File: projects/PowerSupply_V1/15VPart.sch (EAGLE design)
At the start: 24 parts, among them IC1 LM2596T, IC2 LM2596T, X1 IN, X2 OUT

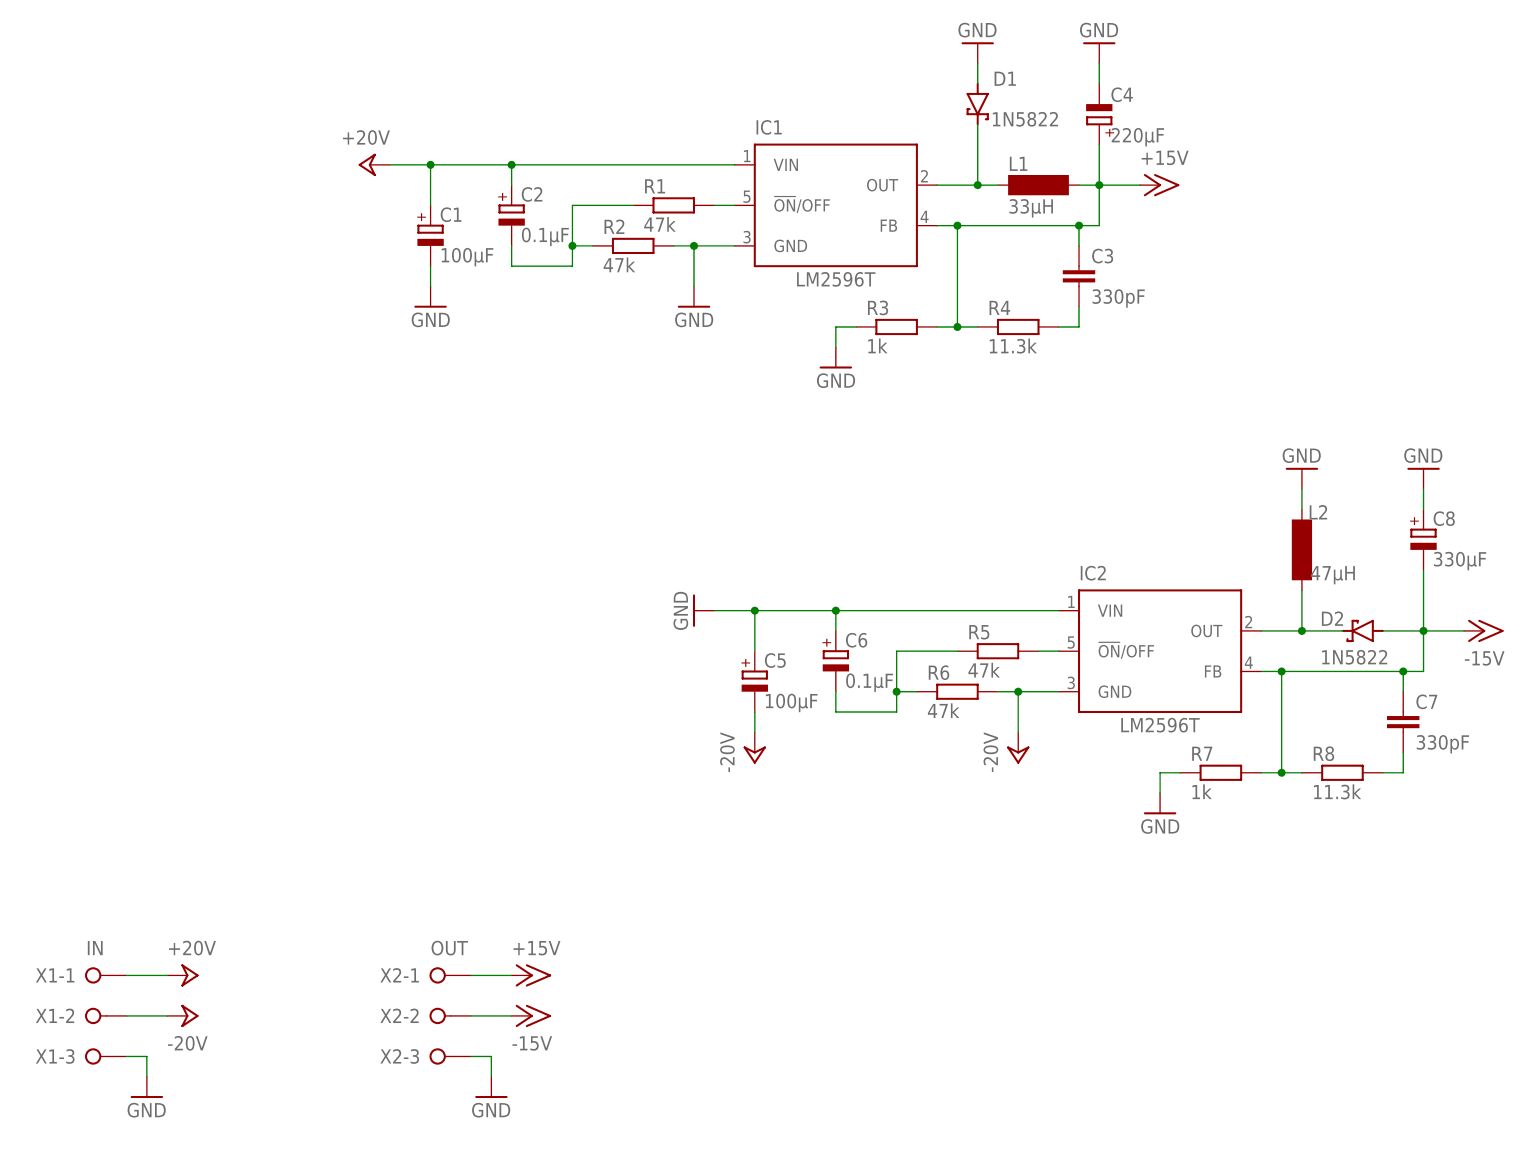
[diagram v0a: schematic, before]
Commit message: refactor(15v): schematics and routing changed
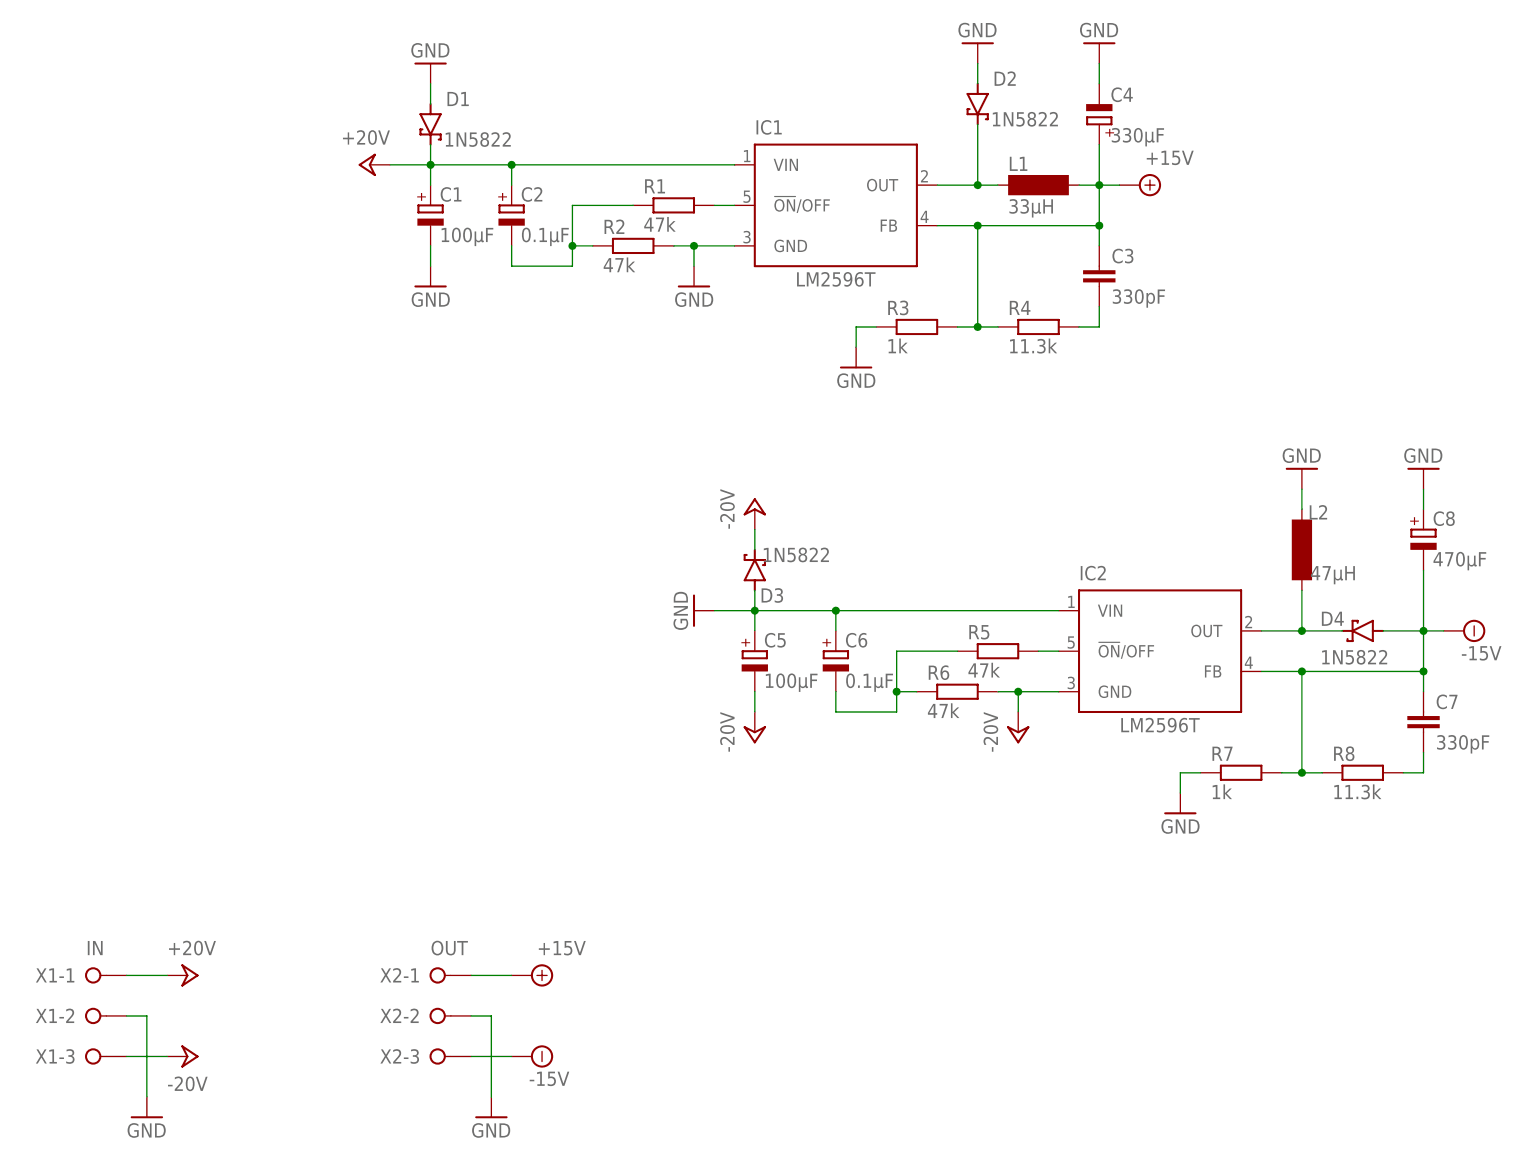
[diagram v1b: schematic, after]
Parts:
- added D3, D4: 1N5822, diode:SCHOTTKY-DIODEC4111-15
- C4: value 220µF -> 330µF
- C8: value 330µF -> 470µF
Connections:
- net +24V: now also D1.C
- net -15V: now also D4.A, X2-3.KL; no longer D2.A, X2-2.KL
- net -24V: now also D3.C, X1-3.KL; no longer X1-2.KL
- net GND: now also D2.A, D3.A, X1-2.KL, X2-2.KL; no longer X1-3.KL, X2-3.KL
- net N$2: now also D4.C; no longer D2.C
- net N$3: now also D2.C; no longer D1.C
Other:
- moved on the sheet: C1, C3, C5, C7, D1, D2, R3, R4, R7, R8

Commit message: feat: 15VPart refactored
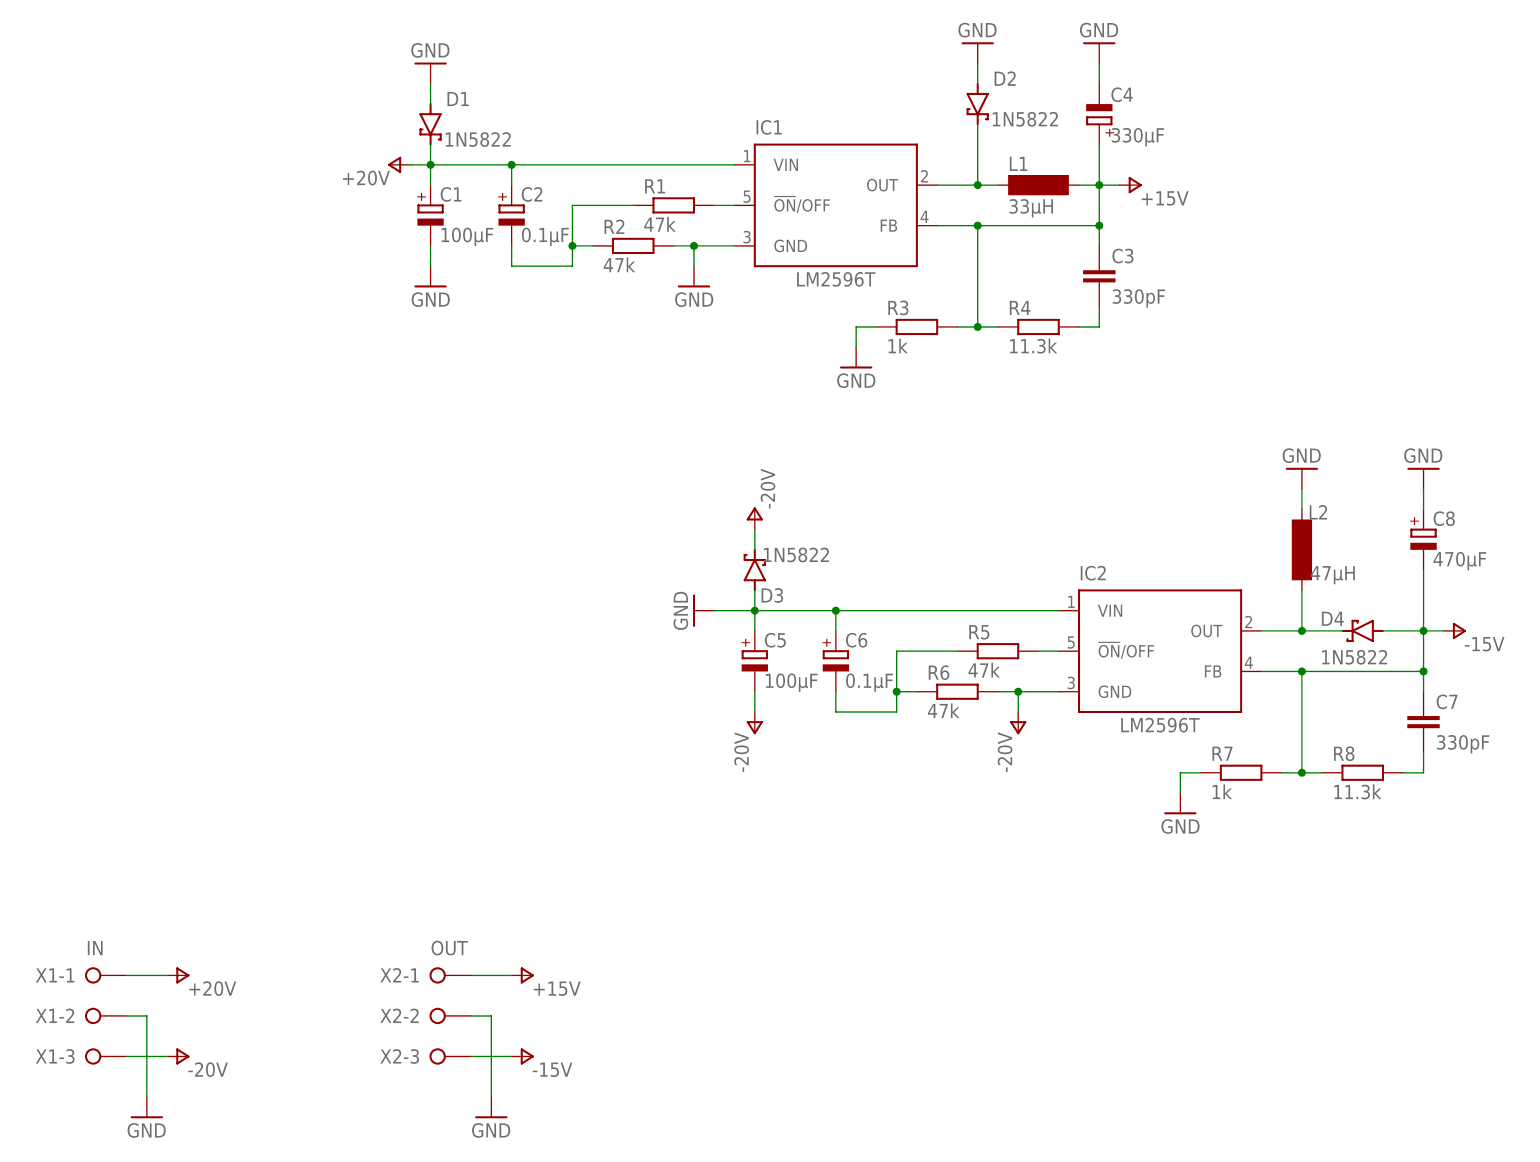
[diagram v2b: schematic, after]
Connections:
- net +24V renamed +20V
- net -24V renamed -20V
